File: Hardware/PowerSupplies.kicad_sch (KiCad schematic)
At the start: 56 parts, among them P1 XT60PW-M, P2 XT60PW-F, P3 XT60PW-F, P4 XT60PW-F, P5 XT60PW-F, U1 LM3414, U2 SY8303, U3 LM3414, U4 SY8303, U5 LM3414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

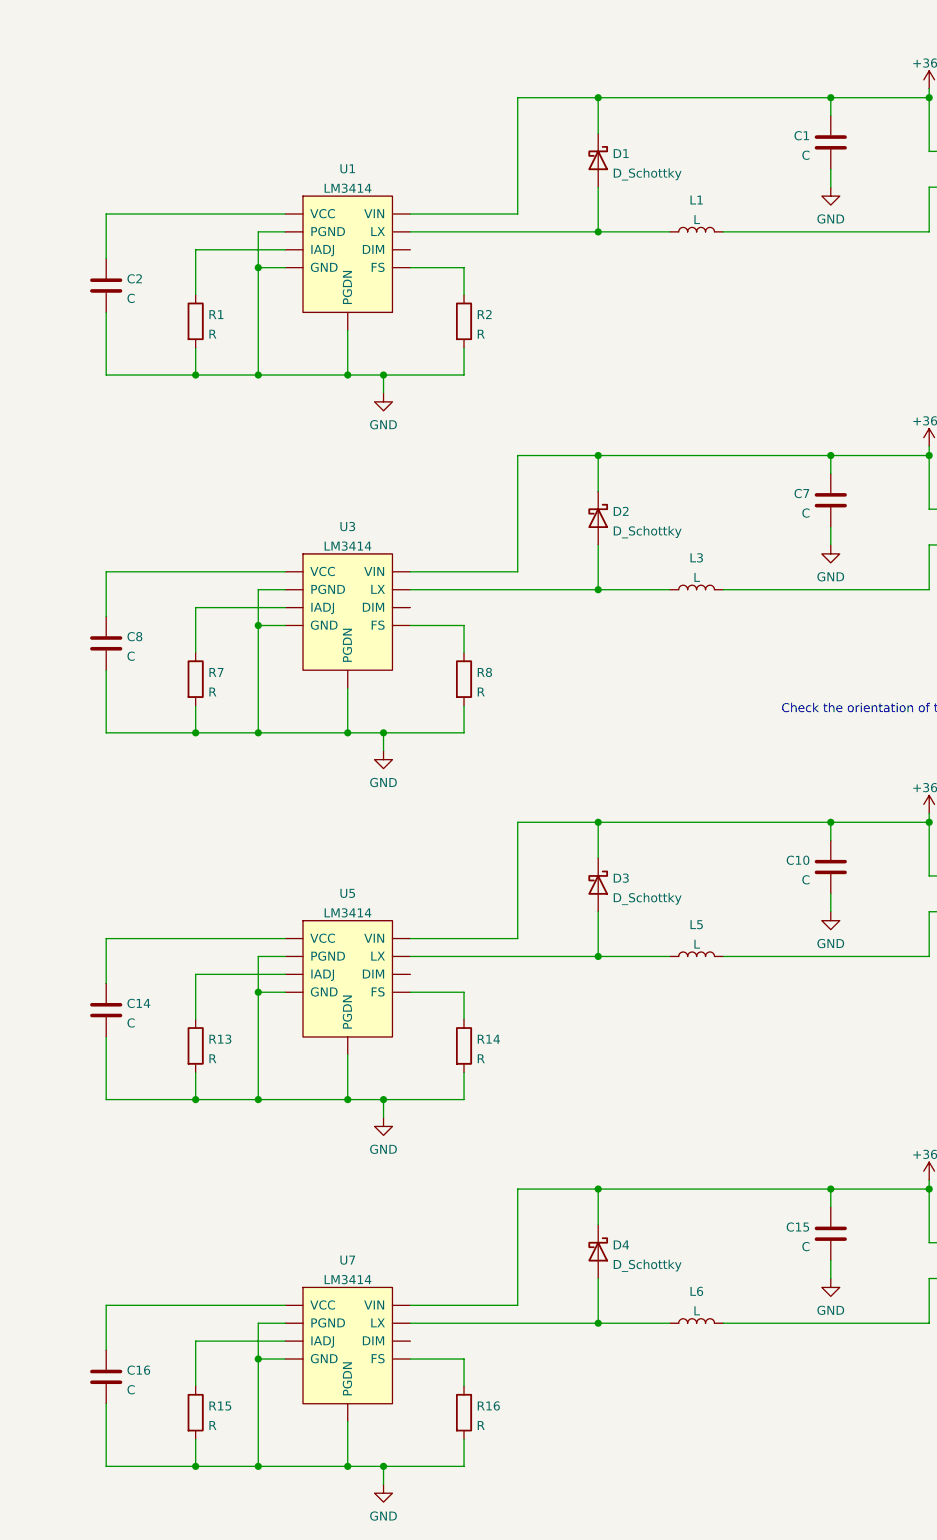
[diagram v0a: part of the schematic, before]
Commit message: LED driver part values & labels on IO page
Added the values (and some part numbers) for the LED drivers, and added some floating labels on the IO sheet to remind what still needs connecting.
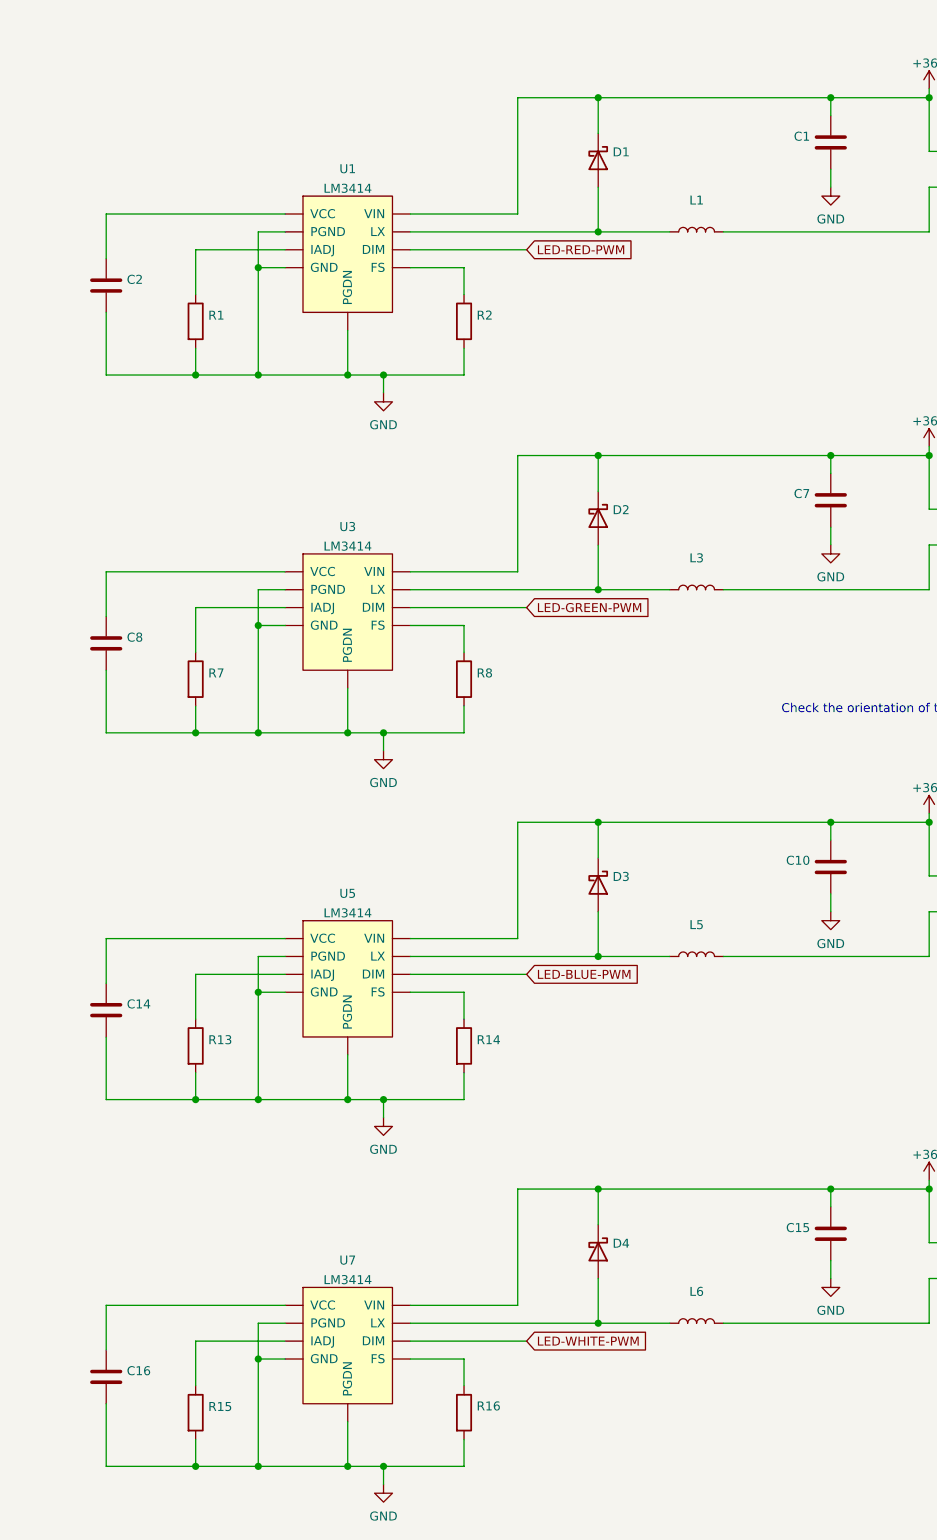
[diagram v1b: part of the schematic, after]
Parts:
- C1, C10, C15, C7: value C -> (none); Part_number (none) -> RVT2A2R2M0605
- C14, C16, C2, C8: value C -> (none)
- D1, D2, D3, D4: value D_Schottky -> (none)
- L1, L3, L5, L6: value L -> (none); Part_number (none) -> SMDR104R-330MT
- R1, R13, R14, R15, R16, R2, R7, R8: value R -> (none)
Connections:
- net LED-WHITE-PWM: now reaches U7.6 (DIM)
- net LED-RED-PWM: now reaches U1.6 (DIM)
- net LED-GREEN-PWM: now reaches U3.6 (DIM)
- net LED-BLUE-PWM: now reaches U5.6 (DIM)

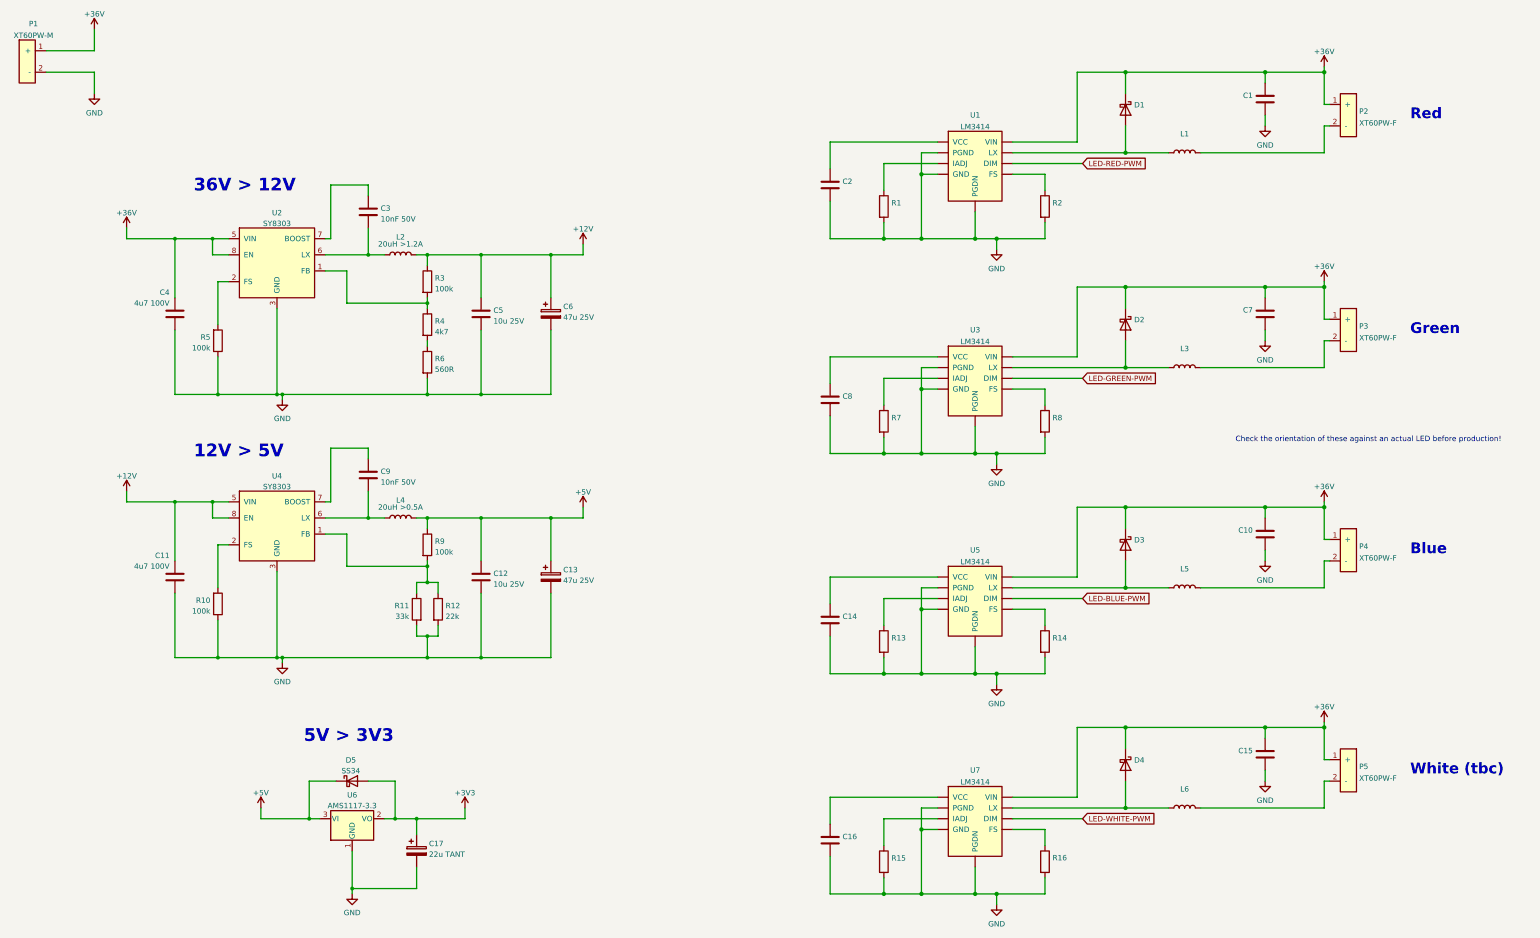
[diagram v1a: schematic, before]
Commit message: Most part assignents made, pending switch footprint & xtal selection
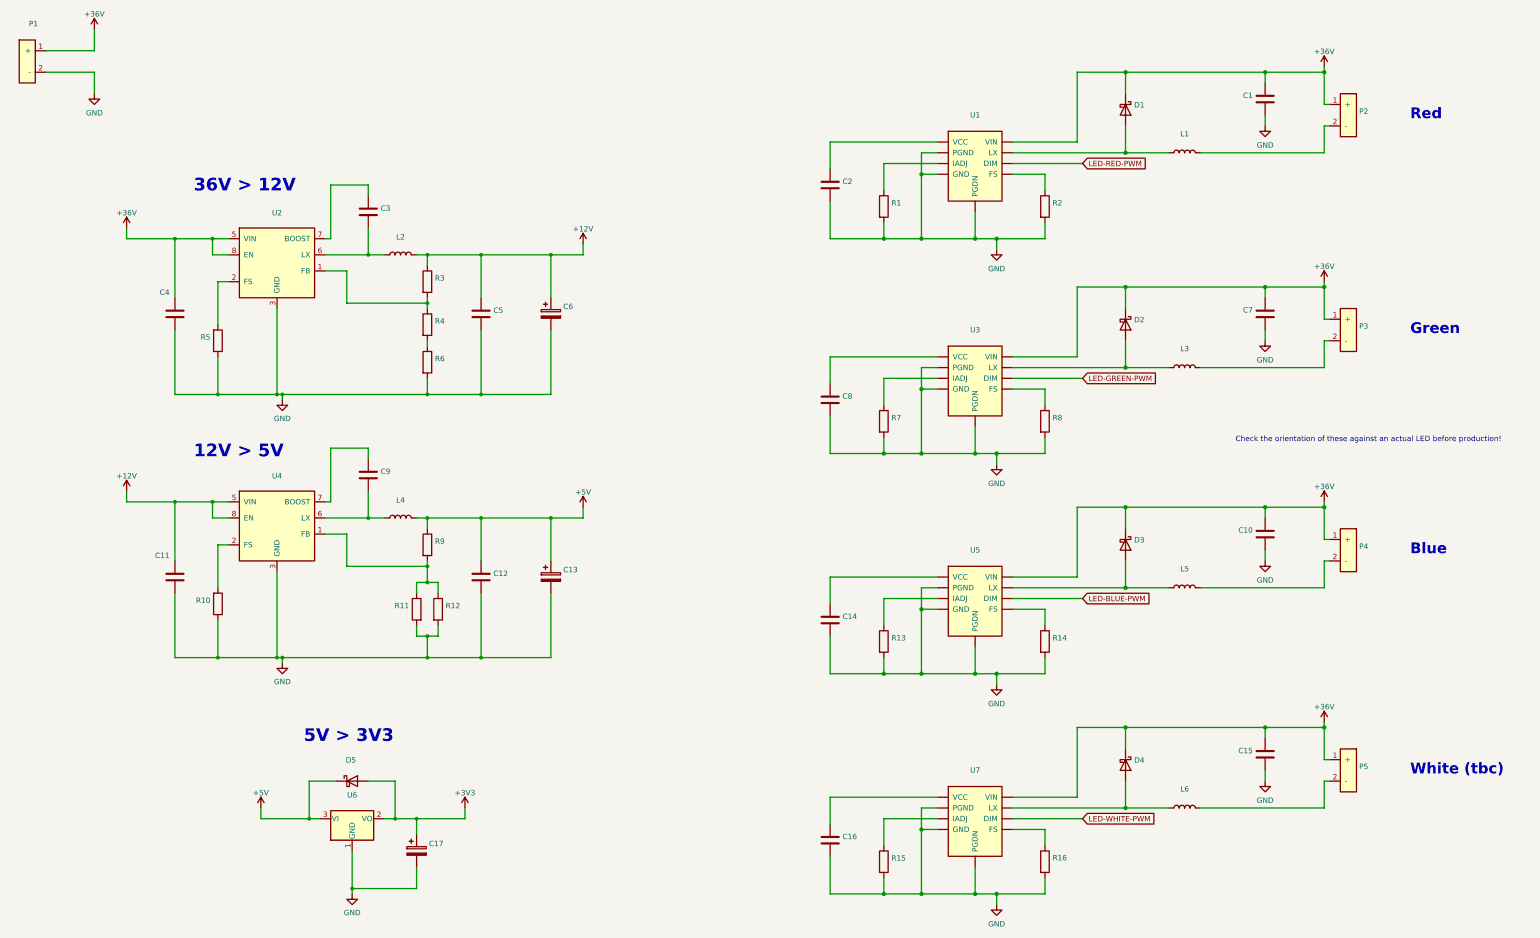
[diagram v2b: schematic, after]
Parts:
- C11, C4: value 4u7 100V -> (none); footprint Capacitor_SMD:C_1206_3216Metric_Pad1.33x1.80mm_HandSolder -> (none); Part_number (none) -> HMK325C7475KN-TE
- C12, C5: value 10u 25V -> (none); Part_number (none) -> CL21A106KAYNNNE
- C13, C6: value 47u 25V -> (none); Part_number (none) -> RVT1E470M0605
- C17: value 22u TANT -> (none); Part_number (none) -> TAJB226K016RNJ
- C3, C9: value 10nF 50V -> (none)
- D1, D2, D3, D4: Part_number (none) -> SS310
- D5: value SS34 -> (none); Part_number (none) -> SS34
- L1, L3, L5, L6: Part_number SMDR104R-330MT -> P0751.333NLT
- L2: value 20uH >1.2A -> (none); Part_number (none) -> NR8040T220M
- L4: value 20uH >0.5A -> (none); Part_number (none) -> NR8040T220M
- P1: value XT60PW-M -> (none); footprint PersonalConnectors:AMASS_XT60PW-M -> (none)
- P2, P3, P4, P5: value XT60PW-F -> (none); footprint PersonalConnectors:AMASS_XT60PW-F -> (none)
- R10, R3, R5, R9: value 100k -> (none)
- R11: value 33k -> (none)
- R12: value 22k -> (none)
- R4: value 4k7 -> (none)
- R6: value 560R -> (none)
- U1, U3, U5, U7: value LM3414 -> (none); footprint PersonalDiscretes:TI_SO-PowerPAD-8_HandSolder -> (none)
- U2, U4: value SY8303 -> (none)
- U6: value AMS1117-3.3 -> (none); footprint Package_TO_SOT_SMD:SOT-223-3_TabPin2 -> (none)
